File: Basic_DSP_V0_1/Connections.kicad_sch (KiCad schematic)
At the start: 46 parts, among them J10 53048-0310, J13 USB_C_Receptacle, J14 53048-0210, J15 53048-0210, J16 Conn_02x08_Odd_Even, J2 53048-0310, J3 53048-0310, J4 53048-0310, J5 53048-0310, J7 53048-0310, J8 53048-0310, J9 53048-0310

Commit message: Minor updates to Basic schematic
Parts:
- removed D10, D11, D12, D13, D22, D24, D4, D5, D7, D8: PESD3V3Z1BSFYL, symbol Chase_Diode:PESD3V3Z1BSFYL
- removed D21: ESD5Z5.0T1G/T5G, Diode_SMD:D_SOD-523, symbol Diode:ESD5Zxx
- added D10, D11, D12, D13, D22, D25, D4, D5, D7, D8: ESD9B3.3ST5G, Diode_SMD:D_SOD-923, symbol Diode:ESD9B3.3ST5G
- added D21: ESD9B5.0ST5G, Diode_SMD:D_SOD-923, symbol Diode:ESD9B5.0ST5G
- C23, C24, C30, C31, C35, C37, C39, C40: footprint Capacitor_SMD:C_0402_1005Metric -> Capacitor_SMD:C_0603_1608Metric_Pad1.08x0.95mm_HandSolder
- R12, R13, R18, R19, R21, R23, R26, R27, R39, R40, R41, R42: footprint Resistor_SMD:R_0402_1005Metric_Pad0.72x0.64mm_HandSolder -> Resistor_SMD:R_0603_1608Metric_Pad0.98x0.95mm_HandSolder
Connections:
- net GND: now also D10.1 (A1), D11.1 (A1), D12.1 (A1), D13.1 (A1), D21.1 (A1), D22.1 (A1), D25.1 (A1), D4.1 (A1), D5.1 (A1), D7.1 (A1), D8.1 (A1)
- net SWITCH_0: now also D13.2 (A2)
- net SWITCH_1: now also D22.2 (A2)
- net VBUS: now also D21.2 (A2)
- net at J2.2, R12.2: now also D25.2 (A2)
- net at J10.2, R27.2: now also D11.2 (A2)
- net at J9.2, R26.2: now also D12.2 (A2)
- net at J8.2, R23.2: now also D10.2 (A2)
- net at J7.2, R21.2: now also D8.2 (A2)
- net at J4.2, R18.2: now also D7.2 (A2)
- net at J3.2, R13.2: now also D4.2 (A2)
- net at J5.2, R19.2: now also D5.2 (A2)
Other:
- note removed: "Check ESD diode order code"

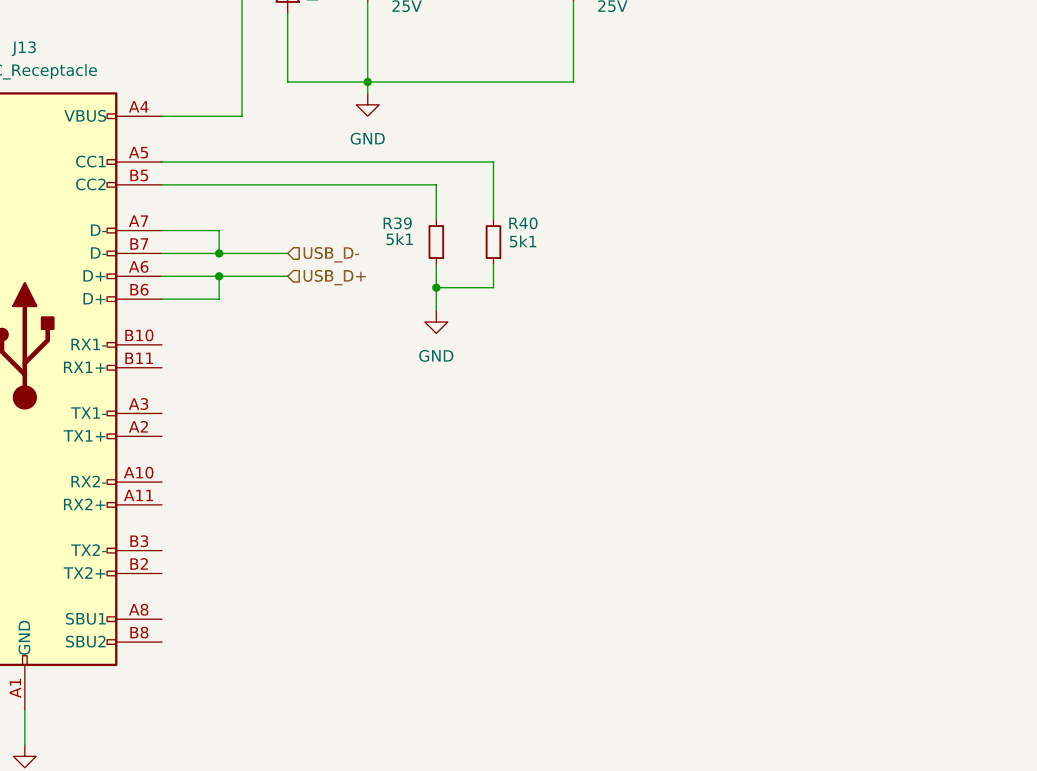
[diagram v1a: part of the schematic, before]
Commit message: Started layout
Removed library from repo as it was messin with the links
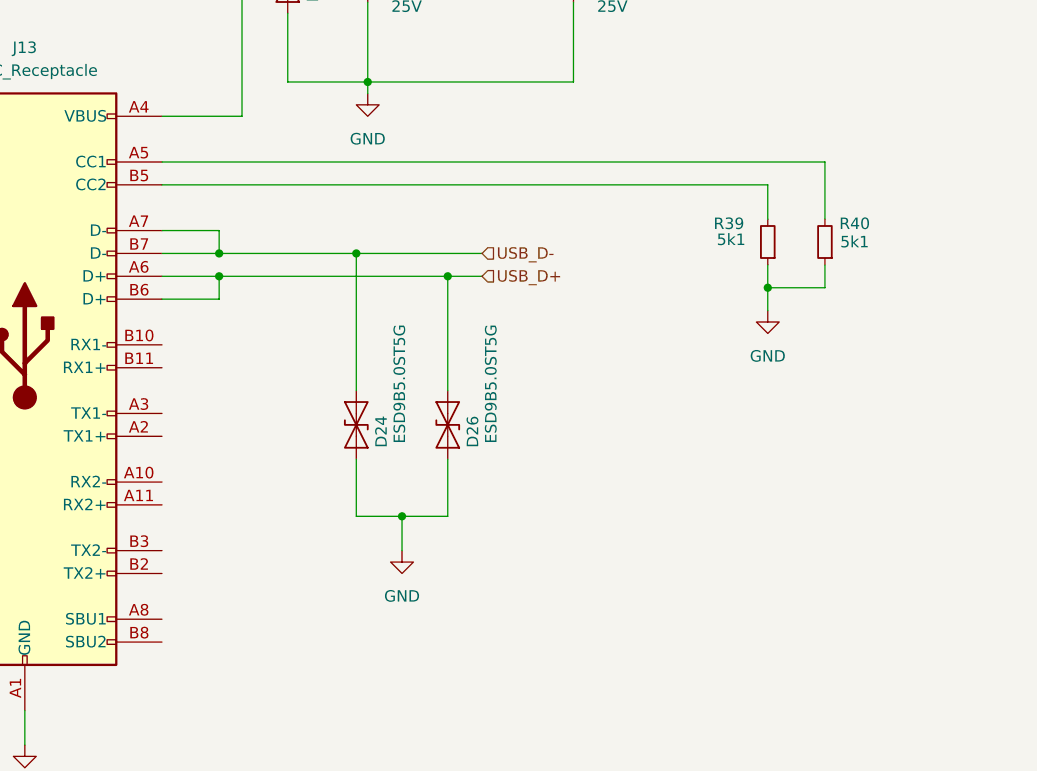
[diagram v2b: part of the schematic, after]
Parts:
- added D24, D26: ESD9B5.0ST5G, Diode_SMD:D_SOD-923, symbol Diode:ESD9B5.0ST5G
- C54, C55: footprint Capacitor_SMD:C_0402_1005Metric -> Capacitor_SMD:C_0603_1608Metric_Pad1.08x0.95mm_HandSolder
- J14, J15: footprint (none) -> Chase_Conn:SHDRRA2W35P0X125_1X2_425X550X350P
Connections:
- net GND: now also D24.1 (A1), D26.1 (A1)
- net USB_D+: now also D26.2 (A2)
- net USB_D-: now also D24.2 (A2)
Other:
- moved on the sheet: R39, R40

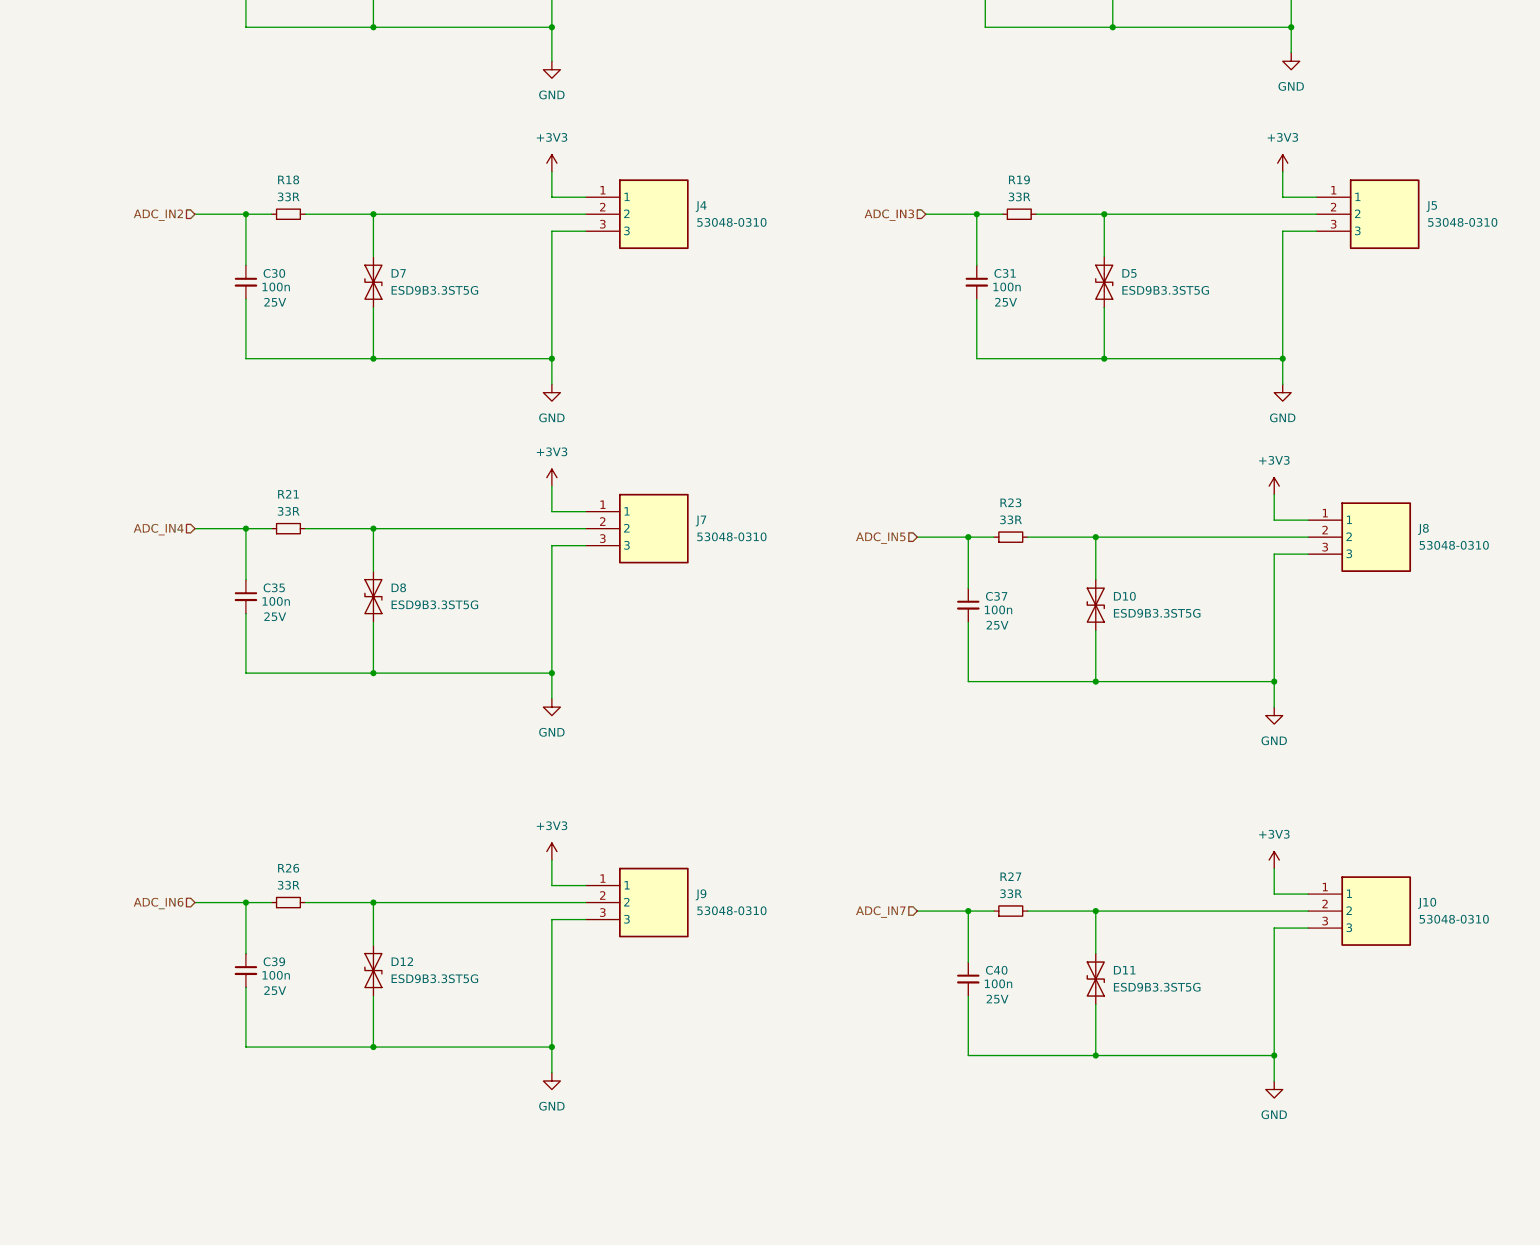
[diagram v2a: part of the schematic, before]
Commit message: Updated parts with LCSC order codes
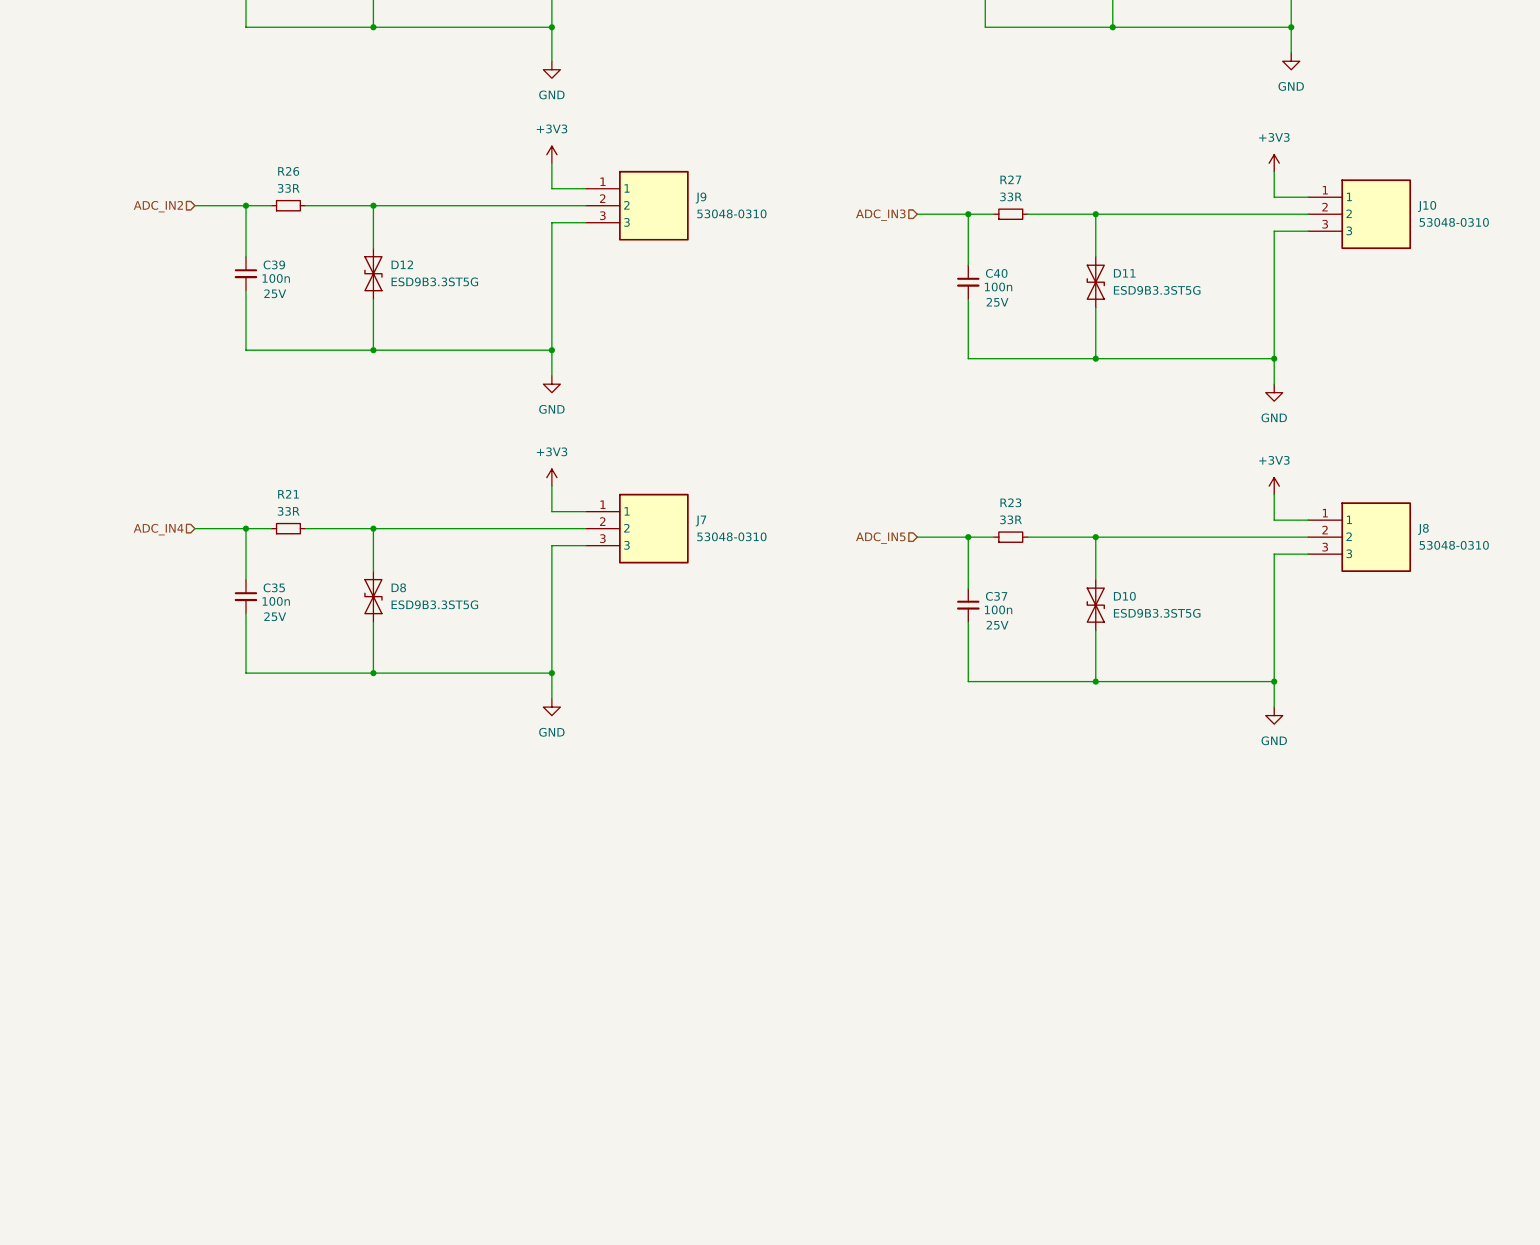
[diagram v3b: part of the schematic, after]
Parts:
- removed C30, C31: 100n, Capacitor_SMD:C_0603_1608Metric_Pad1.08x0.95mm_HandSolder, symbol Device:C_Small
- removed D5, D7: ESD9B3.3ST5G, Diode_SMD:D_SOD-923, symbol Diode:ESD9B3.3ST5G
- removed J4, J5: 53048-0310, Chase_Conn:SHDRRA3W35P0X125_1X3_550X550X350P, symbol Chase_Conn:53048-0310
- removed R18, R19: 33R, Resistor_SMD:R_0603_1608Metric_Pad0.98x0.95mm_HandSolder, symbol Device:R_Small
- C23, C24, C35, C37, C39, C40, C54, C55: MF TAIYO YUDEN -> FH (Guangdong Fenghua Advanced Tech); MPN MBAST105SB7104KFNA01 -> 0603B104M250NT; OC_LCSC (none) -> C336628
- D10, D11, D12, D13, D22, D25, D4, D8: MF (none) -> TECH PUBLIC; MPN (none) -> ESD9B3.3ST5G; OC_LCSC (none) -> C3040608
- D21, D24, D26: MF (none) -> TECH PUBLIC; MPN (none) -> ESD9B5.0ST5G; OC_LCSC (none) -> C3021104
- FB2: OC_LCSC (none) -> C85831
- J10, J2, J3, J7, J8, J9: MF (none) -> MOLEX; MPN (none) -> 530480310; OC_LCSC (none) -> C505275
- J13: MF (none) -> MOLEX; MPN (none) -> 1054500101; OC_LCSC (none) -> C134092
- J14, J15: MF (none) -> MOLEX; MPN (none) -> 530480210; OC_LCSC (none) -> C505099
- J16: MF (none) -> DNP
- R12, R13, R21, R23, R26, R27: MF (none) -> Walsin Tech Corp; MPN (none) -> WR06X33R0FTL; OC_LCSC (none) -> C163909
- R39, R40: MF (none) -> UNI-ROYAL(Uniroyal Elec); MPN (none) -> 0603WAF5101T5E; OC_LCSC (none) -> C23186
- R41, R42: MF (none) -> YAGEO; MPN (none) -> RC0603FR-07100KL; OC_LCSC (none) -> C14675
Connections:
- net ADC_IN6 is gone; now on net ADC_IN2: C39.1, R26.1
- net ADC_IN7 is gone; now on net ADC_IN3: C40.1, R27.1
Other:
- moved on the sheet: C39, C40, D11, D12, J10, J9, R26, R27

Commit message: WIP - small layout progress on basic DSP
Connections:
- net +3.3V is gone; now on net +3V3: J16.2 (Pin_2), R41.1, R42.1
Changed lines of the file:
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@@
 			)
 		)
-		(property "Value" "+3.3V"
+		(property "Value" "+3V3"
 			(at 107.95 236.22 0)
 			(effects
@@
 			)
 		)
-		(property "Value" "+3.3V"
+		(property "Value" "+3V3"
 			(at 374.65 295.91 0)
 			(effects
@@
 			)
 		)
-		(property "Value" "+3.3V"
+		(property "Value" "+3V3"
 			(at 106.68 300.99 0)
 			(effects
